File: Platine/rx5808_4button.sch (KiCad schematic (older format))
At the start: 54 parts, among them IC1 ATMEGA328-A, P1 CONN_01X04, P2 CONN_01X05, P6 CONN_01X04, P7 CONN_02X05, U1 TPS62160, U2 RX5808, U3 sn74lvc1g3157, U4 MCPL3-BC-V, Y1 16 MHz

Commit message: BOM fertiggestellt und alten Code gelöscht
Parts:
- D5: Digikeynummer (none) -> 1080-1379-1-ND
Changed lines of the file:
@@
 F 2 "LEDs:LED_1206" H 5300 7300 50  0001 C CNN
 F 3 "" H 5300 7300 50  0000 C CNN
+F 4 "1080-1379-1-ND" V 5300 7300 60  0001 C CNN "Digikeynummer"
 	1    5300 7300
 	0    -1   -1   0

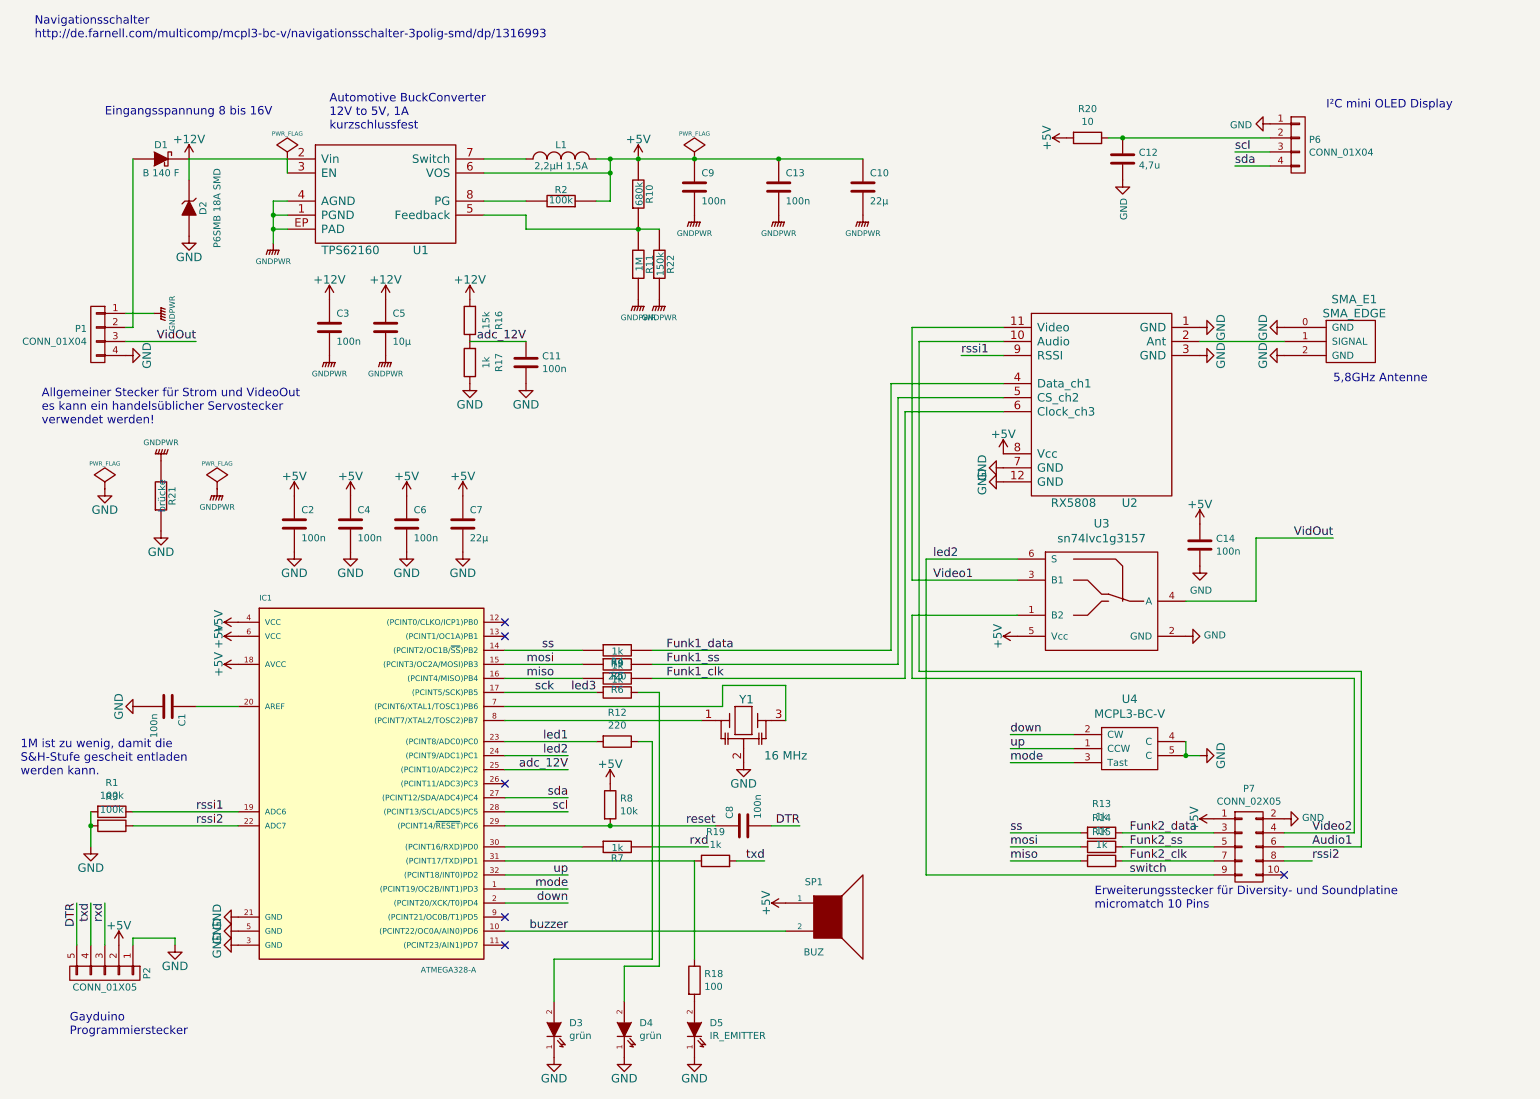
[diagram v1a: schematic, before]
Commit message: Hexfile vom alten Code gelöscht und README-md weitergeschrieben
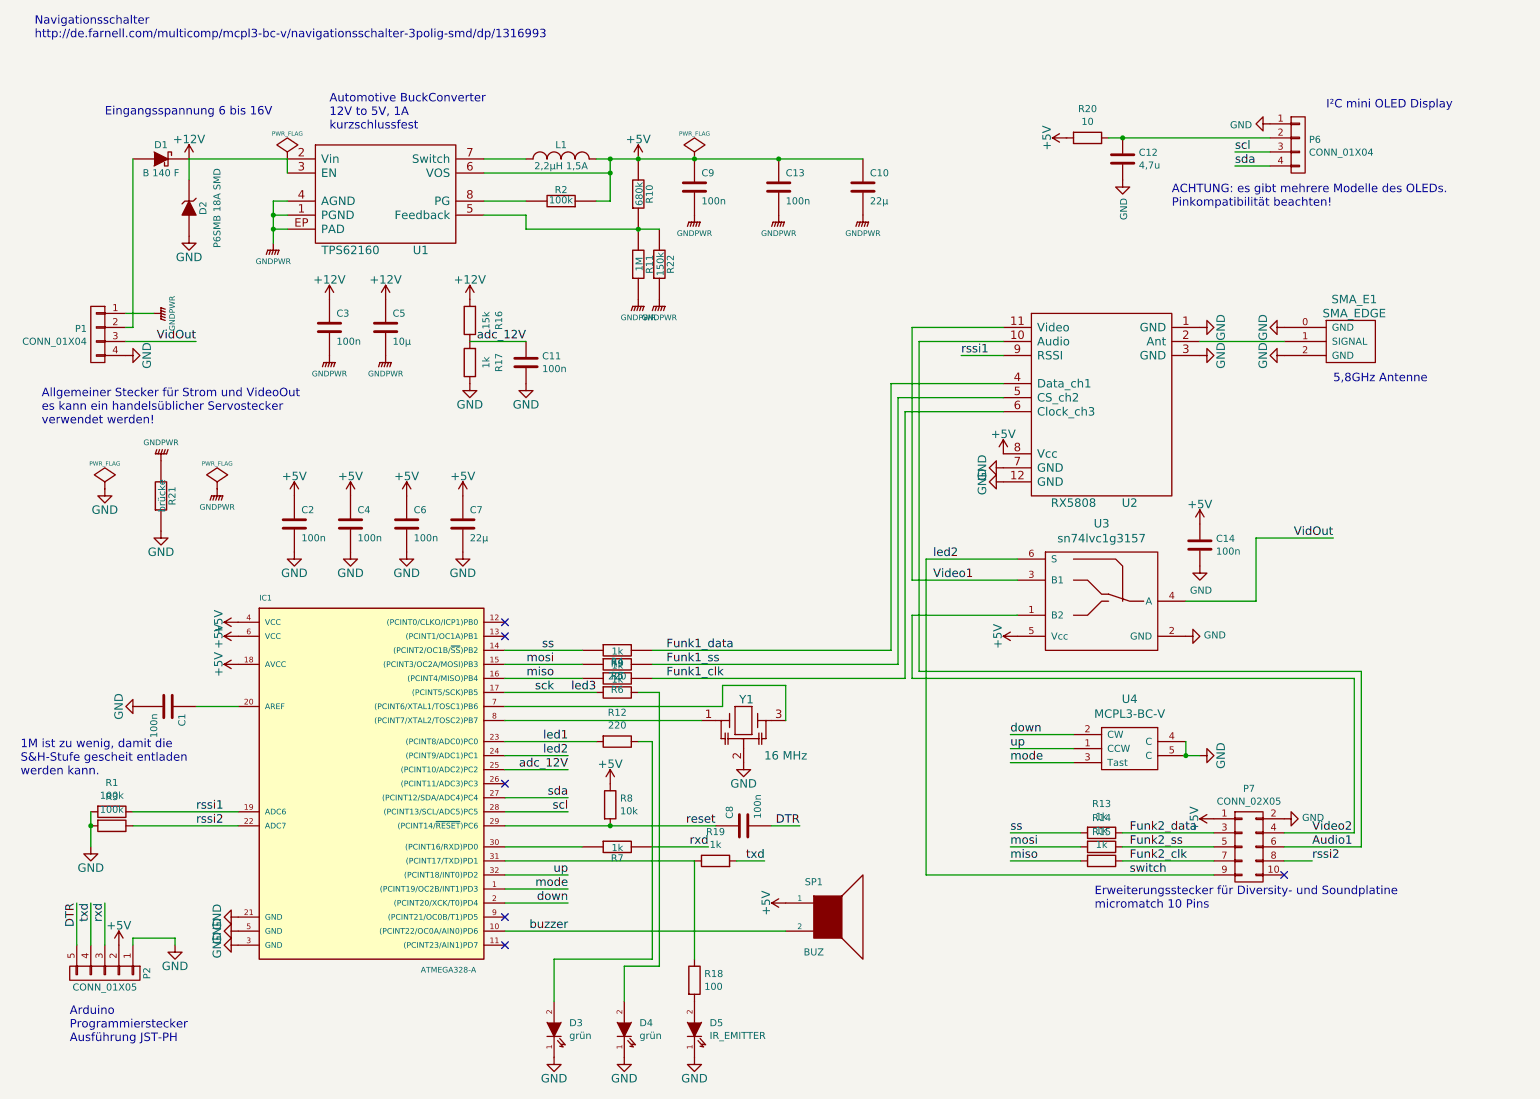
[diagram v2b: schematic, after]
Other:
- note added: "ACHTUNG: es gibt mehrere Modelle des OLEDs.\nPinkompatibilität beachten!"
- note added: "Arduino\nProgrammierstecker\nAusführung JST-PH"
- note added: "Eingangsspannung 6 bis 16V"
- note removed: "Eingangsspannung 8 bis 16V"
- note removed: "Gayduino\nProgrammierstecker"
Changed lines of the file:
@@
 	0    1    1    0
 $EndComp
-Text Notes 850  7350 0    60   ~ 0
-Gayduino\nProgrammierstecker
+Text Notes 850  7400 0    60   ~ 0
+Arduino\nProgrammierstecker\nAusführung JST-PH
 NoConn ~ 3950 5550
 Text Label 1750 5750 0    60   ~ 0
@@
 $EndComp
 Text Notes 1100 800  0    60   ~ 0
-Eingangsspannung 8 bis 16V
+Eingangsspannung 6 bis 16V
 Text Notes 2700 900  0    60   ~ 0
 Automotive BuckConverter\n12V to 5V, 1A\nkurzschlussfest
@@
 $EndComp
 $Comp
-L GND #PWR068
+L GND #PWR067
 U 1 1 575693C2
 P 8350 1250
-F 0 "#PWR068" H 8350 1000 50  0001 C CNN
+F 0 "#PWR067" H 8350 1000 50  0001 C CNN
 F 1 "GND" V 8358 1122 50  0000 R CNN
 F 2 "" H 8350 1250 50  0000 C CNN
@@
 Wire Wire Line
 	8800 5350 8900 5350
+Text Notes 8700 1450 0    60   ~ 0
+ACHTUNG: es gibt mehrere Modelle des OLEDs.\nPinkompatibilität beachten!
 $EndSCHEMATC
